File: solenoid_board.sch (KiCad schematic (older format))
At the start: 52 parts, among them J2 MCU_LEFT_LEGS, J3 MCU_RIGHT_LEGS

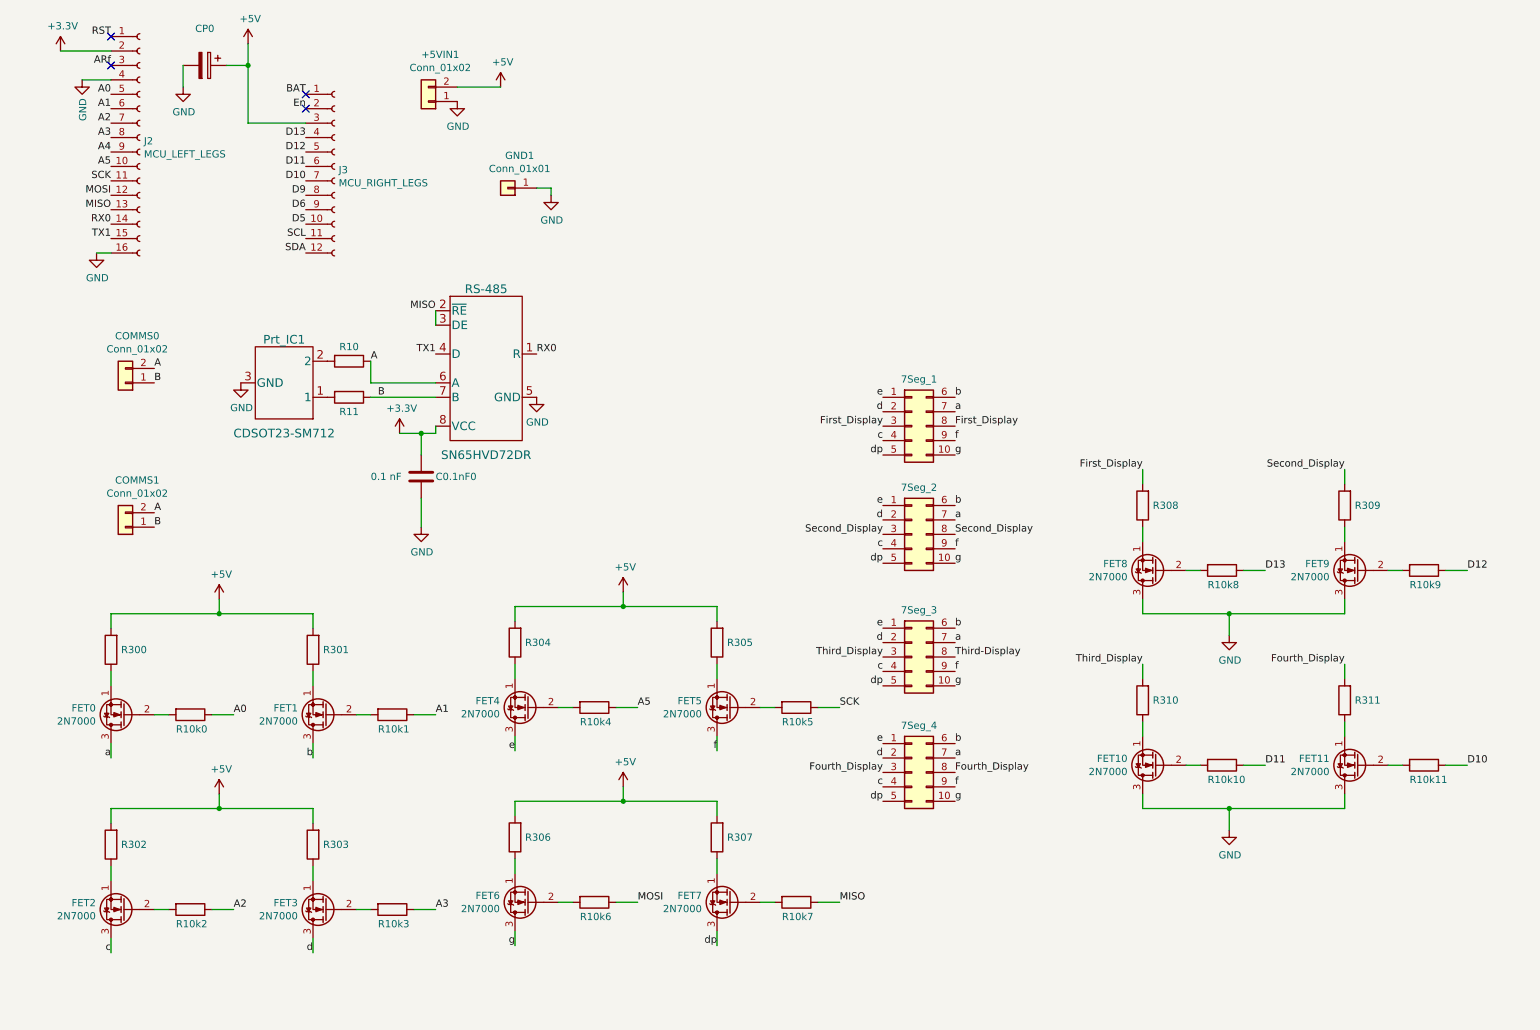
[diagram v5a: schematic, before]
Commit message: Schematic Finished. Need to figure out geometry and route layout.
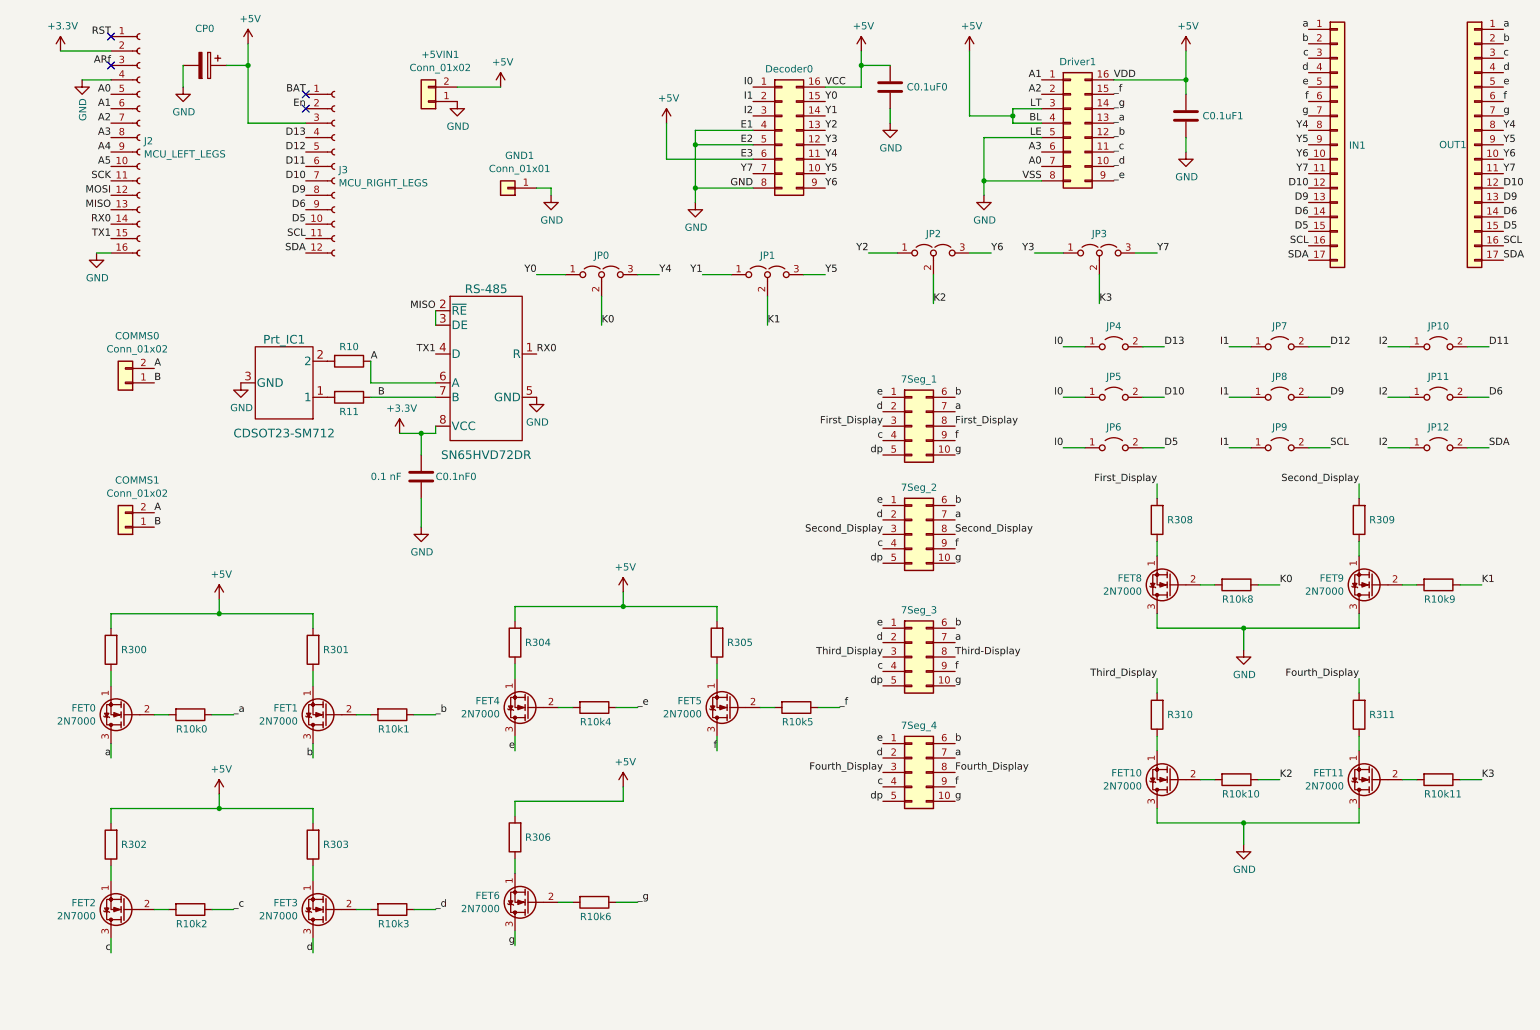
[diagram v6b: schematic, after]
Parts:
- removed FET7: 2N7000, Package_TO_SOT_THT:TO-92_Inline, symbol Transistor_FET:2N7000
- removed R10k7: 10k, Resistor_THT:R_Axial_DIN0204_L3.6mm_D1.6mm_P5.08mm_Vertical, symbol Device:R
- removed R307: 300, Resistor_THT:R_Axial_DIN0204_L3.6mm_D1.6mm_P5.08mm_Vertical, symbol Device:R
- added C0.1uF0, C0.1uF1: 0.1 uF, Capacitor_THT:CP_Radial_D4.0mm_P2.00mm, symbol Device:C
- added Decoder0, Driver1: Conn_02x08_Counter_Clockwise, digikey-footprints:DIP-16_W7.62mm, symbol Connector_Generic:Conn_02x08_Counter_Clockwise
- added IN1, OUT1: Conn_01x17, Connector_PinHeader_2.54mm:PinHeader_1x17_P2.54mm_Vertical, symbol Connector_Generic:Conn_01x17
- added JP0, JP1, JP2, JP3: Jumper_3_Open, Jumper:SolderJumper-3_P1.3mm_Open_RoundedPad1.0x1.5mm, symbol Jumper:Jumper_3_Open
- added JP10, JP11, JP12, JP4, JP5, JP6, JP7, JP8, JP9: Jumper_2_Open, Jumper:SolderJumper-2_P1.3mm_Open_RoundedPad1.0x1.5mm, symbol Jumper:Jumper_2_Open
- R10, R11: footprint Resistor_THT:R_Axial_DIN0309_L9.0mm_D3.2mm_P20.32mm_Horizontal -> Resistor_THT:R_Axial_DIN0204_L3.6mm_D1.6mm_P5.08mm_Vertical
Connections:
- net +5V: now also C0.1uF0.1, C0.1uF1.1, Decoder0.16 (Pin_16), Decoder0.6 (Pin_6), Driver1.16 (Pin_16), Driver1.3 (Pin_3), Driver1.4 (Pin_4)
- net A0: now also Driver1.7 (Pin_7); no longer R10k0.1
- net A1: now also Driver1.1 (Pin_1); no longer R10k1.1
- net A2: now also Driver1.2 (Pin_2); no longer R10k2.1
- net A3: now also Driver1.6 (Pin_6); no longer R10k3.1
- net A5: no longer R10k4.1
- net D10: now also IN1.12 (Pin_12), JP5.2 (B), OUT1.12 (Pin_12); no longer R10k11.1
- net D11: now also JP10.2 (B); no longer R10k10.1
- net D12: now also JP7.2 (B); no longer R10k9.1
- net D13: now also JP4.2 (B); no longer R10k8.1
- net D5: now also IN1.15 (Pin_15), JP6.2 (B), OUT1.15 (Pin_15)
- net D6: now also IN1.14 (Pin_14), JP11.2 (B), OUT1.14 (Pin_14)
- net D9: now also IN1.13 (Pin_13), JP8.2 (B), OUT1.13 (Pin_13)
- net GND: now also C0.1uF0.2, C0.1uF1.2, Decoder0.4 (Pin_4), Decoder0.5 (Pin_5), Decoder0.8 (Pin_8), Driver1.5 (Pin_5), Driver1.8 (Pin_8)
- net MOSI: no longer R10k6.1
- net SCK: no longer R10k5.1
- net SCL: now also IN1.16 (Pin_16), JP9.2 (B), OUT1.16 (Pin_16)
- net SDA: now also IN1.17 (Pin_17), JP12.2 (B), OUT1.17 (Pin_17)
- net a: now also IN1.1 (Pin_1), OUT1.1 (Pin_1)
- net b: now also IN1.2 (Pin_2), OUT1.2 (Pin_2)
- net c: now also IN1.3 (Pin_3), OUT1.3 (Pin_3)
- net d: now also IN1.4 (Pin_4), OUT1.4 (Pin_4)
- net e: now also IN1.5 (Pin_5), OUT1.5 (Pin_5)
- net f: now also IN1.6 (Pin_6), OUT1.6 (Pin_6)
- net g: now also IN1.7 (Pin_7), OUT1.7 (Pin_7)
- new net I0: Decoder0.1 (Pin_1), JP4.1 (A), JP5.1 (A), JP6.1 (A)
- new net I1: Decoder0.2 (Pin_2), JP7.1 (A), JP8.1 (A), JP9.1 (A)
- new net I2: Decoder0.3 (Pin_3), JP10.1 (A), JP11.1 (A), JP12.1 (A)
- new net K0: JP0.2 (C), R10k8.1
- new net K1: JP1.2 (C), R10k9.1
- new net K2: JP2.2 (C), R10k10.1
- new net K3: JP3.2 (C), R10k11.1
- new net Y0: Decoder0.15 (Pin_15), JP0.1 (A)
- new net Y1: Decoder0.14 (Pin_14), JP1.1 (A)
- new net Y2: Decoder0.13 (Pin_13), JP2.1 (A)
- new net Y3: Decoder0.12 (Pin_12), JP3.1 (A)
- new net Y4: Decoder0.11 (Pin_11), IN1.8 (Pin_8), JP0.3 (B), OUT1.8 (Pin_8)
- new net Y5: Decoder0.10 (Pin_10), IN1.9 (Pin_9), JP1.3 (B), OUT1.9 (Pin_9)
- new net Y6: Decoder0.9 (Pin_9), IN1.10 (Pin_10), JP2.3 (B), OUT1.10 (Pin_10)
- new net Y7: Decoder0.7 (Pin_7), IN1.11 (Pin_11), JP3.3 (B), OUT1.11 (Pin_11)
- new net _a: Driver1.13 (Pin_13), R10k0.1
- new net _b: Driver1.12 (Pin_12), R10k1.1
- new net _c: Driver1.11 (Pin_11), R10k2.1
- new net _d: Driver1.10 (Pin_10), R10k3.1
- new net _e: Driver1.9 (Pin_9), R10k4.1
- new net _f: Driver1.15 (Pin_15), R10k5.1
- new net _g: Driver1.14 (Pin_14), R10k6.1
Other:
- moved on the sheet: FET10, FET11, FET8, FET9, R10k10, R10k11, R10k8, R10k9, R308, R309, R310, R311

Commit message: Worked Geometry to 40% mark.
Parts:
- removed C0.1uF1: 0.1 uF, Capacitor_THT:CP_Radial_D4.0mm_P2.00mm, symbol Device:C
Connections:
- net Y4: now also IN1.11 (Pin_11), OUT1.11 (Pin_11); no longer IN1.8 (Pin_8), OUT1.8 (Pin_8)
- net Y5: now also IN1.10 (Pin_10), OUT1.10 (Pin_10); no longer IN1.9 (Pin_9), OUT1.9 (Pin_9)
- net Y6: now also IN1.9 (Pin_9), OUT1.9 (Pin_9); no longer IN1.10 (Pin_10), OUT1.10 (Pin_10)
- net Y7: now also IN1.8 (Pin_8), OUT1.8 (Pin_8); no longer IN1.11 (Pin_11), OUT1.11 (Pin_11)
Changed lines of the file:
@@
-$EndComp
-Wire Wire Line
-	8650 1400 8650 1500
-$Comp
-L power:GND #PWR0122
-U 1 1 5E6D9799
-P 8650 1500
-F 0 "#PWR0122" H 8650 1250 50  0001 C CNN
-F 1 "GND" H 8655 1327 50  0000 C CNN
-F 2 "" H 8650 1500 50  0001 C CNN
-F 3 "" H 8650 1500 50  0001 C CNN
-	1    8650 1500
-	1    0    0    -1
-$EndComp
-$Comp
-L Device:C C0.1uF1
-U 1 1 5E6D979F
-P 8650 1250
-F 0 "C0.1uF1" H 8765 1250 50  0000 L CNN
-F 1 "0.1 uF" H 8765 1205 50  0001 L CNN
-F 2 "Capacitor_THT:CP_Radial_D4.0mm_P2.00mm" H 8688 1100 50  0001 C CNN
-F 3 "~" H 8650 1250 50  0001 C CNN
-	1    8650 1250
-	1    0    0    -1
 $EndComp
 Wire Wire Line
@@
 Wire Wire Line
 	7150 800  7150 1250
-Wire Wire Line
-	8650 1100 8650 1000
-Connection ~ 8650 1000
 Wire Wire Line
 	5050 1300 5050 1550
@@
 g
 Text Label 9500 1650 2    50   ~ 0
+Y4
+Text Label 9500 1550 2    50   ~ 0
+Y5
+Text Label 9500 1450 2    50   ~ 0
+Y6
+Text Label 9500 1350 2    50   ~ 0
 Y7
-Text Label 9500 1550 2    50   ~ 0
-Y6
-Text Label 9500 1450 2    50   ~ 0
-Y5
-Text Label 9500 1350 2    50   ~ 0
-Y4
 Text Label 9500 1750 2    50   ~ 0
 D10
@@
 g
 Text Label 10850 1650 0    50   ~ 0
+Y4
+Text Label 10850 1550 0    50   ~ 0
+Y5
+Text Label 10850 1450 0    50   ~ 0
+Y6
+Text Label 10850 1350 0    50   ~ 0
 Y7
-Text Label 10850 1550 0    50   ~ 0
-Y6
-Text Label 10850 1450 0    50   ~ 0
-Y5
-Text Label 10850 1350 0    50   ~ 0
-Y4
 Text Label 10850 1750 0    50   ~ 0
 D10
